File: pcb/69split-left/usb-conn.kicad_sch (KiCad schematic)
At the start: 6 parts, among them J3 USB_C_Receptacle_USB2.0_14P

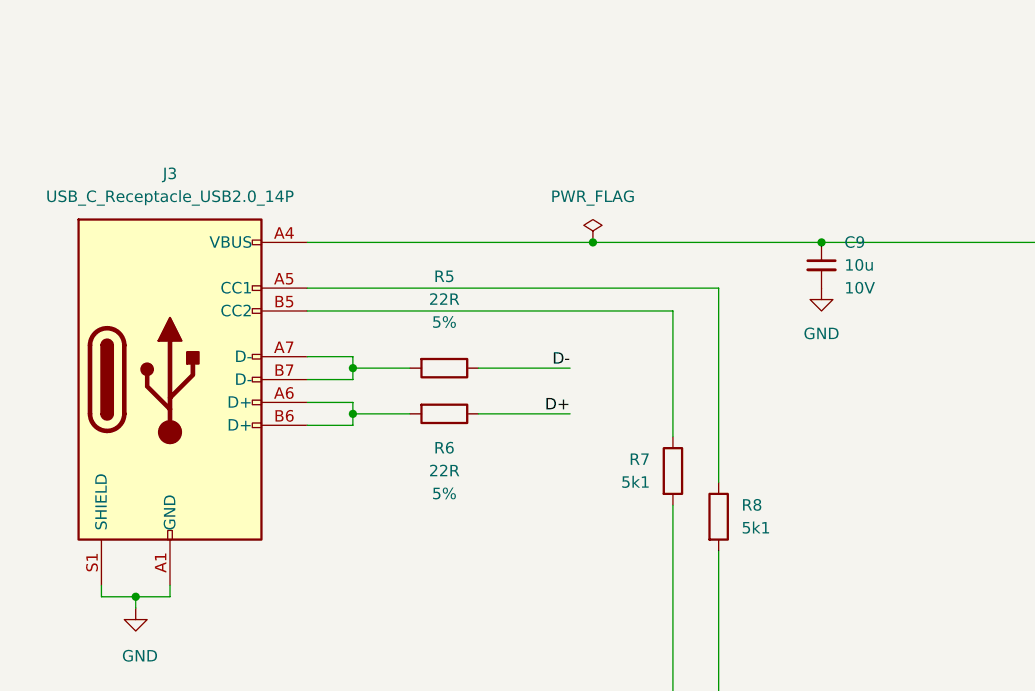
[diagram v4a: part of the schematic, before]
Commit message: Started changing things gain to use an I/O expander with I2C.
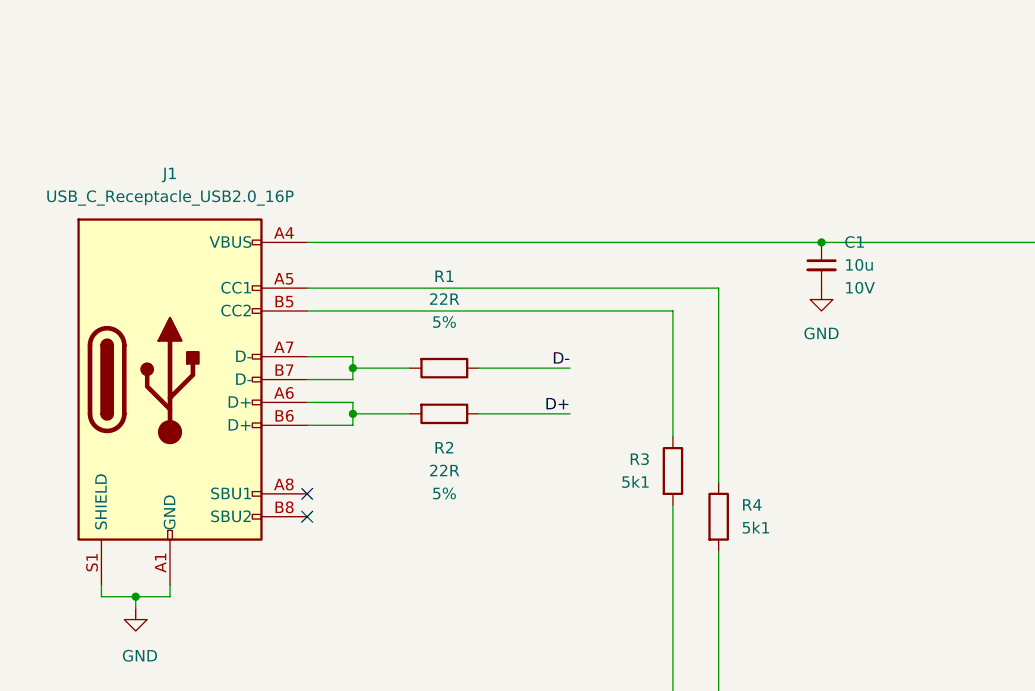
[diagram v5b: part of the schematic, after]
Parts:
- J1: renamed from J3; value USB_C_Receptacle_USB2.0_14P -> USB_C_Receptacle_USB2.0_16P; symbol Connector:USB_C_Receptacle_USB2.0_14P -> Connector:USB_C_Receptacle_USB2.0_16P
- renumbered C9 to C1, R5 to R1, R6 to R2, R7 to R3, R8 to R4
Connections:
- no-connect marks 0 -> 2
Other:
- company: (none) -> Yiannis Michael
- title: 69SPLIT KEYBOARD -> 69SPLIT
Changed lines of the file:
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@@
 	(paper "A4")
 	(title_block
-		(title "69SPLIT KEYBOARD")
-		(date "2025-06-21")
+		(title "69SPLIT")
+		(date "2025-07-28")
 		(rev "1")
+		(company "Yiannis Michael")
 		(comment 1 "Yiannis Michael")
 		(comment 2 "ymich9963")
@@
 	)
 	(junction
-		(at 143.51 78.74)
-		(diameter 0)
-		(color 0 0 0 0)
-	)
-	(junction
 		(at 92.71 118.11)
 		(diameter 0)
@@
 		(color 0 0 0 0)
 	)
+	(no_connect
+		(at 111.76 106.68)
+	)
+	(no_connect
+		(at 111.76 109.22)
+	)
 	(bus_entry
 		(at 226.06 99.06)
@@
 	(wire
 		(pts
-			(xy 143.51 78.74) (xy 168.91 78.74)
-		)
-		(stroke
-			(width 0)
-			(type default)
-		)
-	)
-	(wire
-		(pts
-			(xy 111.76 78.74) (xy 143.51 78.74)
+			(xy 111.76 78.74) (xy 168.91 78.74)
 		)
 		(stroke
@@
 		(dnp no)
 		(fields_autoplaced yes)
-		(property "Reference" "R5"
+		(property "Reference" "R1"
 			(at 127 82.55 90)
 			(effects
@@
 		)
 		(instances
+			(project "69split"
+				(path "/1573ac28-80e2-4ab2-b20c-1c4896f37ece/800133d0-6e68-49ca-a870-e06397f7c02c/9761ff83-2474-42df-b43e-2f8540936a26"
+					(reference "R?")
+					(unit 1)
+				)
+			)
 			(project "69split-left"
 				(path "/94301c1c-44b1-4926-ac38-8a25b84a2b23/9761ff83-2474-42df-b43e-2f8540936a26"
-					(reference "R5")
+					(reference "R1")
 					(unit 1)
 				)
@@
 		(dnp no)
 		(fields_autoplaced yes)
-		(property "Reference" "R6"
+		(property "Reference" "R2"
 			(at 127 101.6 90)
 			(effects
@@
 		)
 		(instances
+			(project "69split"
+				(path "/1573ac28-80e2-4ab2-b20c-1c4896f37ece/800133d0-6e68-49ca-a870-e06397f7c02c/9761ff83-2474-42df-b43e-2f8540936a26"
+					(reference "R?")
+					(unit 1)
+				)
+			)
 			(project "69split-left"
 				(path "/94301c1c-44b1-4926-ac38-8a25b84a2b23/9761ff83-2474-42df-b43e-2f8540936a26"
-					(reference "R6")
+					(reference "R2")
 					(unit 1)
 				)
@@
 	)
 	(symbol
-		(lib_id "Connector:USB_C_Receptacle_USB2.0_14P")
+		(lib_id "Connector:USB_C_Receptacle_USB2.0_16P")
 		(at 96.52 93.98 0)
 		(unit 1)
@@
 		(dnp no)
 		(fields_autoplaced yes)
-		(property "Reference" "J3"
+		(property "Reference" "J1"
 			(at 96.52 71.12 0)
 			(effects
@@
 			)
 		)
-		(property "Value" "USB_C_Receptacle_USB2.0_14P"
+		(property "Value" "USB_C_Receptacle_USB2.0_16P"
 			(at 96.52 73.66 0)
 			(effects
@@
 			)
 		)
-		(property "Description" "USB 2.0-only 14P Type-C Receptacle connector"
+		(property "Description" "USB 2.0-only 16P Type-C Receptacle connector"
 			(at 96.52 93.98 0)
 			(effects
@@
 		(pin "B6"
 		)
+		(pin "A8"
+		)
+		(pin "B8"
+		)
 		(instances
+			(project "69split"
+				(path "/1573ac28-80e2-4ab2-b20c-1c4896f37ece/800133d0-6e68-49ca-a870-e06397f7c02c/9761ff83-2474-42df-b43e-2f8540936a26"
+					(reference "J?")
+					(unit 1)
+				)
+			)
 			(project "69split-left"
 				(path "/94301c1c-44b1-4926-ac38-8a25b84a2b23/9761ff83-2474-42df-b43e-2f8540936a26"
-					(reference "J3")
+					(reference "J1")
 					(unit 1)
 				)
@@
 		(dnp no)
 		(fields_autoplaced yes)
-		(property "Reference" "#PWR019"
+		(property "Reference" "#PWR02"
 			(at 168.91 90.17 0)
 			(effects
@@
 		)
 		(instances
+			(project "69split"
+				(path "/1573ac28-80e2-4ab2-b20c-1c4896f37ece/800133d0-6e68-49ca-a870-e06397f7c02c/9761ff83-2474-42df-b43e-2f8540936a26"
+					(reference "#PWR?")
+					(unit 1)
+				)
+			)
 			(project "69split-left"
 				(path "/94301c1c-44b1-4926-ac38-8a25b84a2b23/9761ff83-2474-42df-b43e-2f8540936a26"
-					(reference "#PWR019")
+					(reference "#PWR02")
 					(unit 1)
 				)
@@
 		(dnp no)
 		(fields_autoplaced yes)
-		(property "Reference" "R8"
+		(property "Reference" "R4"
 			(at 160.02 107.9499 0)
 			(effects
@@
 		)
 		(instances
+			(project "69split"
+				(path "/1573ac28-80e2-4ab2-b20c-1c4896f37ece/800133d0-6e68-49ca-a870-e06397f7c02c/9761ff83-2474-42df-b43e-2f8540936a26"
+					(reference "R?")
+					(unit 1)
+				)
+			)
 			(project "69split-left"
 				(path "/94301c1c-44b1-4926-ac38-8a25b84a2b23/9761ff83-2474-42df-b43e-2f8540936a26"
-					(reference "R8")
+					(reference "R4")
 					(unit 1)
 				)
@@
 		(dnp no)
 		(fields_autoplaced yes)
-		(property "Reference" "#PWR021"
+		(property "Reference" "#PWR04"
 			(at 154.94 138.43 0)
 			(effects
@@
 		)
 		(instances
+			(project "69split"
+				(path "/1573ac28-80e2-4ab2-b20c-1c4896f37ece/800133d0-6e68-49ca-a870-e06397f7c02c/9761ff83-2474-42df-b43e-2f8540936a26"
+					(reference "#PWR?")
+					(unit 1)
+				)
+			)
 			(project "69split-left"
 				(path "/94301c1c-44b1-4926-ac38-8a25b84a2b23/9761ff83-2474-42df-b43e-2f8540936a26"
-					(reference "#PWR021")
+					(reference "#PWR04")
 					(unit 1)
 				)
@@
 		(dnp no)
 		(fields_autoplaced yes)
-		(property "Reference" "R7"
+		(property "Reference" "R3"
 			(at 149.86 102.8699 0)
 			(effects
@@
 		)
 		(instances
+			(project "69split"
+				(path "/1573ac28-80e2-4ab2-b20c-1c4896f37ece/800133d0-6e68-49ca-a870-e06397f7c02c/9761ff83-2474-42df-b43e-2f8540936a26"
+					(reference "R?")
+					(unit 1)
+				)
+			)
 			(project "69split-left"
 				(path "/94301c1c-44b1-4926-ac38-8a25b84a2b23/9761ff83-2474-42df-b43e-2f8540936a26"
-					(reference "R7")
-					(unit 1)
-				)
-			)
-		)
-	)
-	(symbol
-		(lib_id "power:PWR_FLAG")
-		(at 143.51 78.74 0)
-		(unit 1)
-		(exclude_from_sim no)
-		(in_bom yes)
-		(on_board yes)
-		(dnp no)
-		(fields_autoplaced yes)
-		(property "Reference" "#FLG02"
-			(at 143.51 76.835 0)
-			(effects
-				(font
-					(size 1.27 1.27)
-				)
-				(hide yes)
-			)
-		)
-		(property "Value" "PWR_FLAG"
-			(at 143.51 73.66 0)
-			(effects
-				(font
-					(size 1.27 1.27)
-				)
-			)
-		)
-		(property "Footprint" ""
-			(at 143.51 78.74 0)
-			(effects
-				(font
-					(size 1.27 1.27)
-				)
-				(hide yes)
-			)
-		)
-		(property "Datasheet" "~"
-			(at 143.51 78.74 0)
-			(effects
-				(font
-					(size 1.27 1.27)
-				)
-				(hide yes)
-			)
-		)
-		(property "Description" "Special symbol for telling ERC where power comes from"
-			(at 143.51 78.74 0)
-			(effects
-				(font
-					(size 1.27 1.27)
-				)
-				(hide yes)
-			)
-		)
-		(pin "1"
-		)
-		(instances
-			(project ""
-				(path "/94301c1c-44b1-4926-ac38-8a25b84a2b23/9761ff83-2474-42df-b43e-2f8540936a26"
-					(reference "#FLG02")
+					(reference "R3")
 					(unit 1)
 				)
@@
 		(on_board yes)
 		(dnp no)
-		(property "Reference" "#PWR020"
+		(property "Reference" "#PWR03"
 			(at 92.71 125.73 0)
 			(effects
@@
 		)
 		(instances
+			(project "69split"
+				(path "/1573ac28-80e2-4ab2-b20c-1c4896f37ece/800133d0-6e68-49ca-a870-e06397f7c02c/9761ff83-2474-42df-b43e-2f8540936a26"
+					(reference "#PWR?")
+					(unit 1)
+				)
+			)
 			(project "69split-left"
 				(path "/94301c1c-44b1-4926-ac38-8a25b84a2b23/9761ff83-2474-42df-b43e-2f8540936a26"
-					(reference "#PWR020")
+					(reference "#PWR03")
 					(unit 1)
 				)
@@
 		(dnp no)
 		(fields_autoplaced yes)
-		(property "Reference" "C9"
+		(property "Reference" "C1"
 			(at 171.45 78.7462 0)
 			(effects
@@
 		)
 		(instances
+			(project "69split"
+				(path "/1573ac28-80e2-4ab2-b20c-1c4896f37ece/800133d0-6e68-49ca-a870-e06397f7c02c/9761ff83-2474-42df-b43e-2f8540936a26"
+					(reference "C?")
+					(unit 1)
+				)
+			)
 			(project "69split-left"
 				(path "/94301c1c-44b1-4926-ac38-8a25b84a2b23/9761ff83-2474-42df-b43e-2f8540936a26"
-					(reference "C9")
-					(unit 1)
-				)
+					(reference "C1")
+					(unit 1)
+				)

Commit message: Finished left keyboard again...
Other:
- moved on the sheet: C1, R1, R2, R3, R4

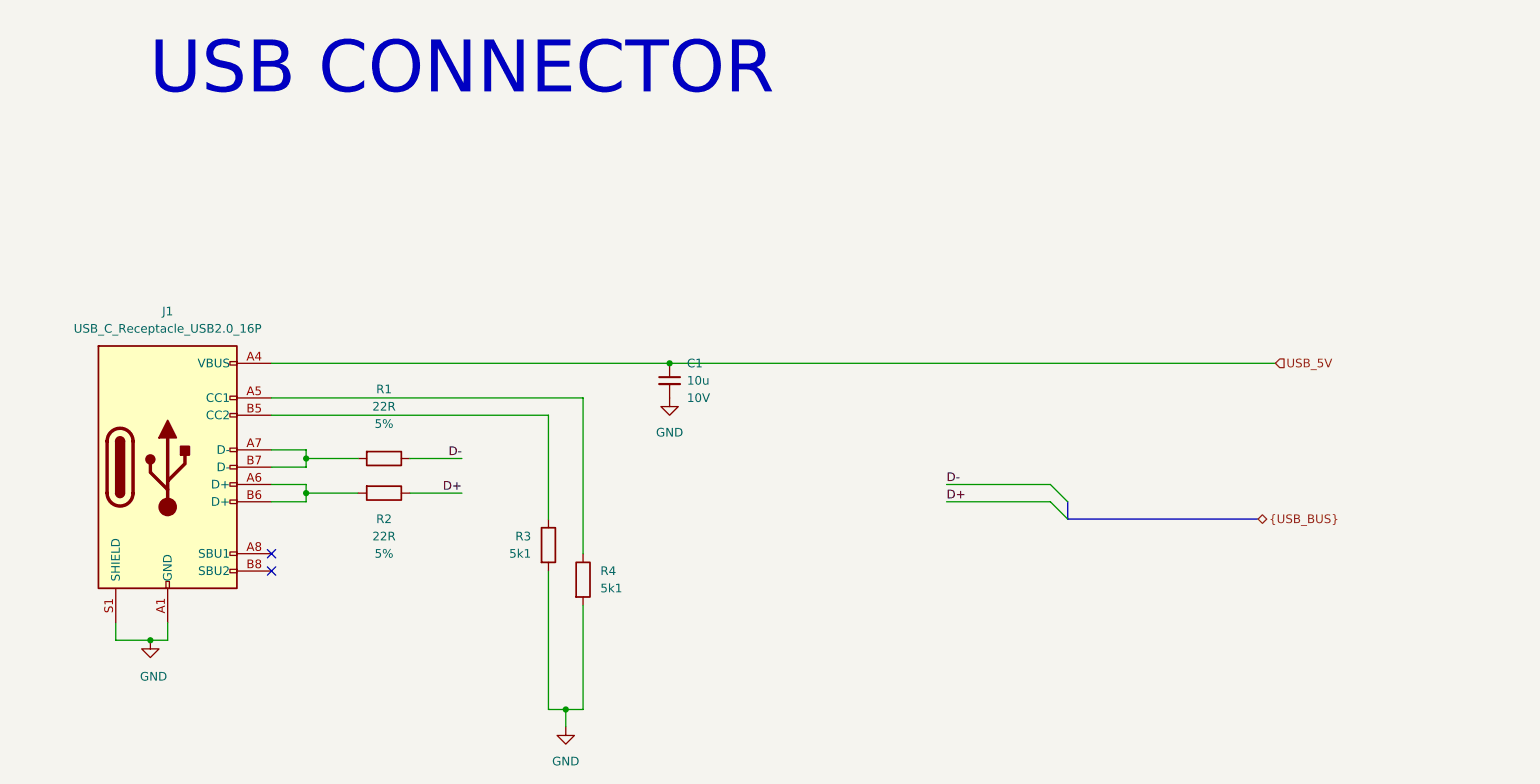
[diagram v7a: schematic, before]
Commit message: Added ESD protection and better routing for the USB data lines.
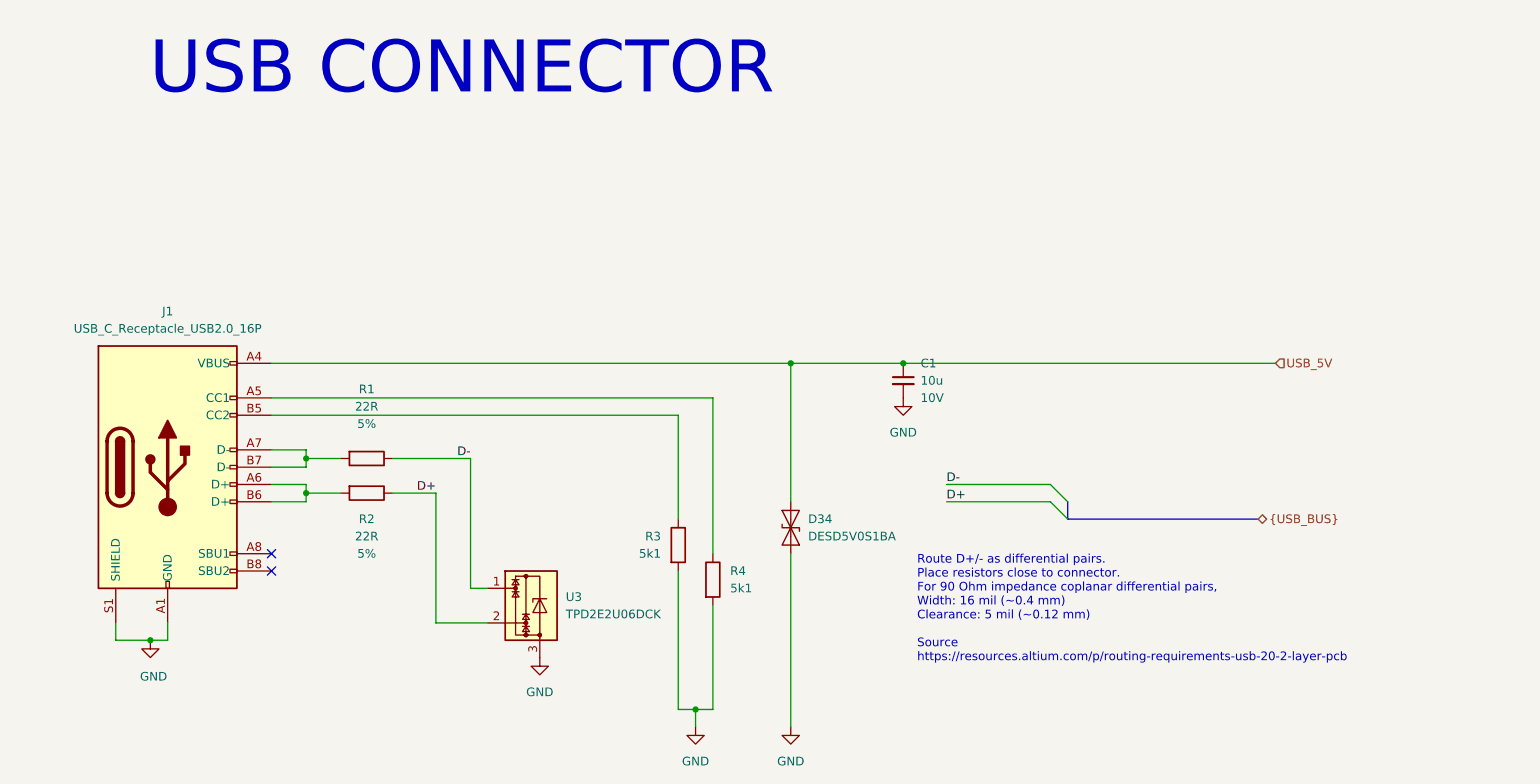
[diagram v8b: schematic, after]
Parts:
- added D34: DESD5V0S1BA, Diode_SMD:D_SOD-323_HandSoldering, symbol Diode:SD05_SOD323
- added U3: TPD2E2U06DCK, Package_TO_SOT_SMD:SOT-323_SC-70, symbol Power_Protection:TPD2E2U06DCK
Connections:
- net D+: now also U3.2
- net D-: now also U3.1
- net GND: now also D34.1 (A1), U3.3
- net USB_5V: now also D34.2 (A2)
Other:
- note added: "Route D+/- as differential pairs. Place resistors close to connector. For 90 Ohm impedance coplanar differential pairs, Width: 16 mil (~0.4 mm) Clearance: 5 mil (~0.12 mm) Source https://resources.altium.com/p/routing-requirements-usb-20-2-layer-pcb"
- moved on the sheet: C1, R1, R2, R3, R4
